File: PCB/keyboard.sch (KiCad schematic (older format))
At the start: 154 parts, among them J1 USB_mini_micro_B, U1 ATMEGA32U4, X1 Crystal_GND24_Small

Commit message: added standard 68 key layout
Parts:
- added D_R_ALT_STD_1: D, acheron_Components:D_SOD-123, symbol Device:D
- added K_BCK_STD1: KEYSW, MX_Only:MXOnly-2U-NoLED, symbol keyboard_parts:KEYSW
- added K_CAPS_STD_2: KEYSW, MX_Only:MXOnly-1.75U-NoLED, symbol keyboard_parts:KEYSW
- added K_CMD_STD_1, K_CMD_STD_3, K_CTRL_STD_1, K_MEN_STD_1, K_R_ALT_STD_1, K_WIN_STD_1: KEYSW, MX_Only:MXOnly-1.25U-NoLED, symbol keyboard_parts:KEYSW
- added K_SPACE_STD1: KEYSW, MX_Only:MXOnly-6.25U-NoLED, symbol keyboard_parts:KEYSW
- K_&lt;I1, K_&lt;I2, K_&lt;I3, K_CTRL1, K_TAB1: footprint MX_Alps_Hybrid:MX-1.5U-NoLED -> MX_Only:MXOnly-1.5U-NoLED
- K_&lt;I_E1, K_0, K_1, K_2, K_3, K_4, K_5, K_6, K_7, K_8, K_9, K_A1, K_B1, K_BSLSH1, K_C1, K_CBRAC1, K_COMMA1, K_D1, K_DELETE1, K_DOT1, K_DOWN1, K_E1, K_END1, K_EQUAL1, K_F1, K_FN1, K_G1, K_H1, K_HOME1, K_I1, K_INSERT1, K_J1, K_K1, K_L1, K_LEFT1, K_M1, K_MINUS1, K_N1, K_O1, K_OBRAC1, K_P1, K_Q1, K_QUOTE1, K_R1, K_RIGHT1, K_S1, K_SEMIC1, K_SLASH1, K_T1, K_U1, K_UP1, K_V1, K_W1, K_X1, K_Y1, K_Z1, K_`1: footprint MX_Alps_Hybrid:MX-1U-NoLED -> MX_Only:MXOnly-1U-NoLED
- K_ALT1, K_CAPS1, K_WIN1: footprint MX_Alps_Hybrid:MX-1.25U-NoLED -> MX_Only:MXOnly-1.25U-NoLED
- K_ENTER1, K_SHIFT2: footprint MX_Alps_Hybrid:MX-2.25U-NoLED -> MX_Only:MXOnly-2.25U-NoLED
- K_SHIFT1: footprint MX_Alps_Hybrid:MX-1.75U-NoLED -> MX_Only:MXOnly-1.75U-NoLED
- K_SPACE1: footprint MX_Alps_Hybrid:MX-7U-NoLED -> MX_Only:MXOnly-7U-NoLED
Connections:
- net col0: now also K_CAPS_STD_2.1, K_CTRL_STD_1.1
- net col11: now also K_R_ALT_STD_1.1
- net col12: now also K_CMD_STD_3.1
- net col13: now also K_BCK_STD1.1
- net col2: now also K_WIN_STD_1.1
- net col3: now also K_CMD_STD_1.1
- net col7: now also K_SPACE_STD1.1
- net at D_CAPS1.2 (A), K_CAPS1.2: now also K_CAPS_STD_2.2
- net at D_CTRL1.2 (A), K_CTRL1.2: now also K_CTRL_STD_1.2
- net at D_WIN1.2 (A), K_WIN1.2: now also K_WIN_STD_1.2
- net at D_&lt;I2.2 (A), K_&lt;I2.2: now also K_CMD_STD_1.2
- net at D_SPACE1.2 (A), K_SPACE1.2: now also K_SPACE_STD1.2
- net at D_&lt;I3.2 (A), K_&lt;I3.2: now also K_CMD_STD_3.2
- net at D_ALT1.2 (A), K_ALT1.2: now also K_MEN_STD_1.2
- net at D_BSLSH1.2 (A), K_BSLSH1.2: now also K_BCK_STD1.2
- new net: D_R_ALT_STD_1.2 (A), K_R_ALT_STD_1.2

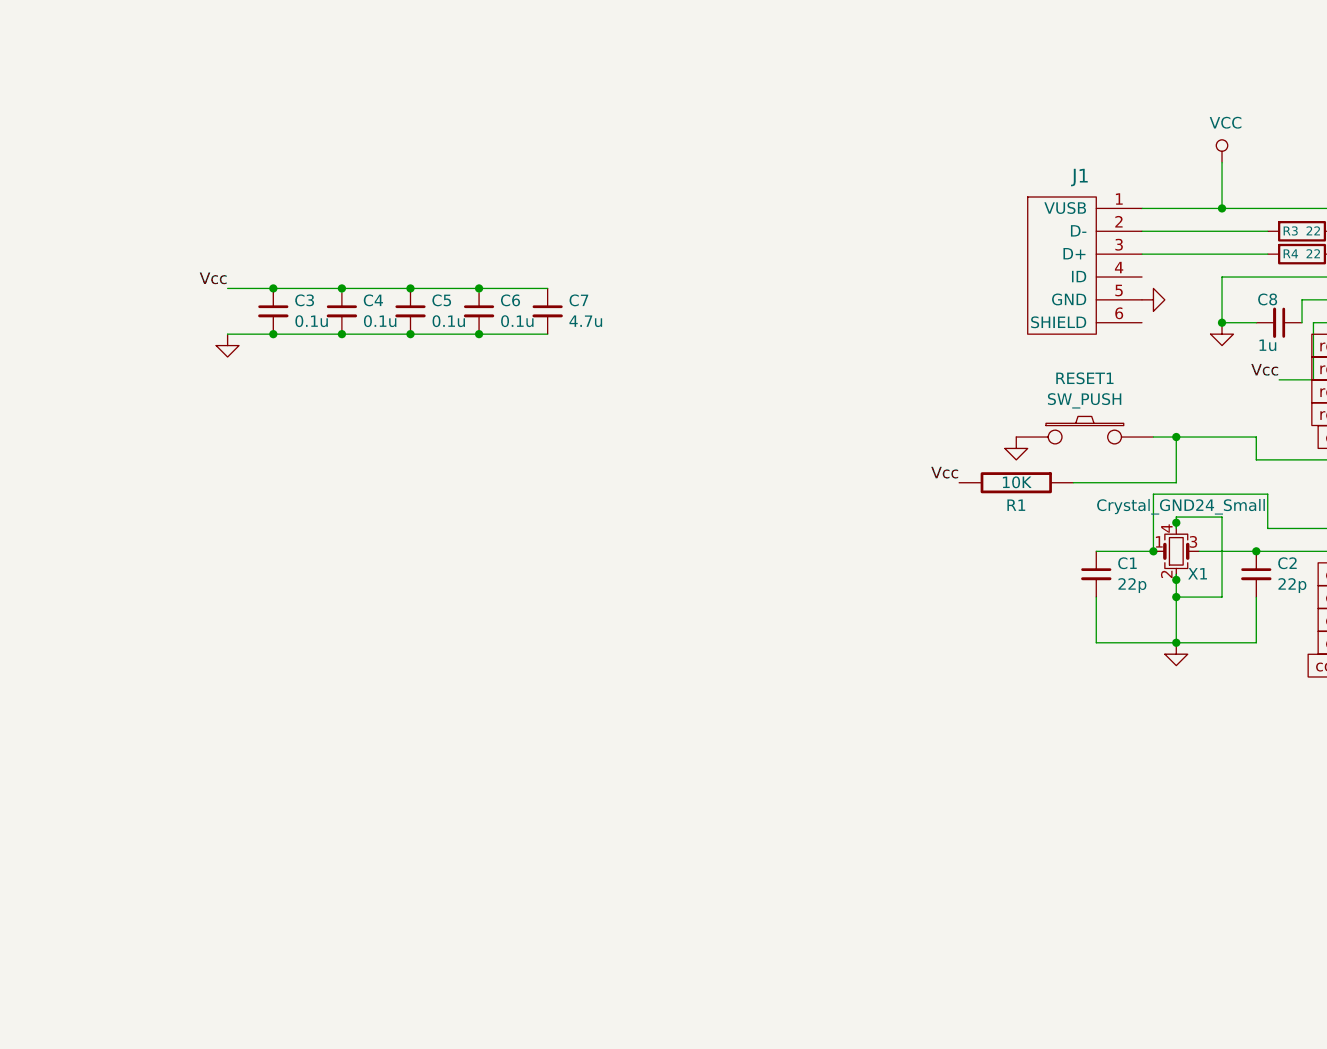
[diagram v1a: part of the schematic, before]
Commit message: added usb type c.
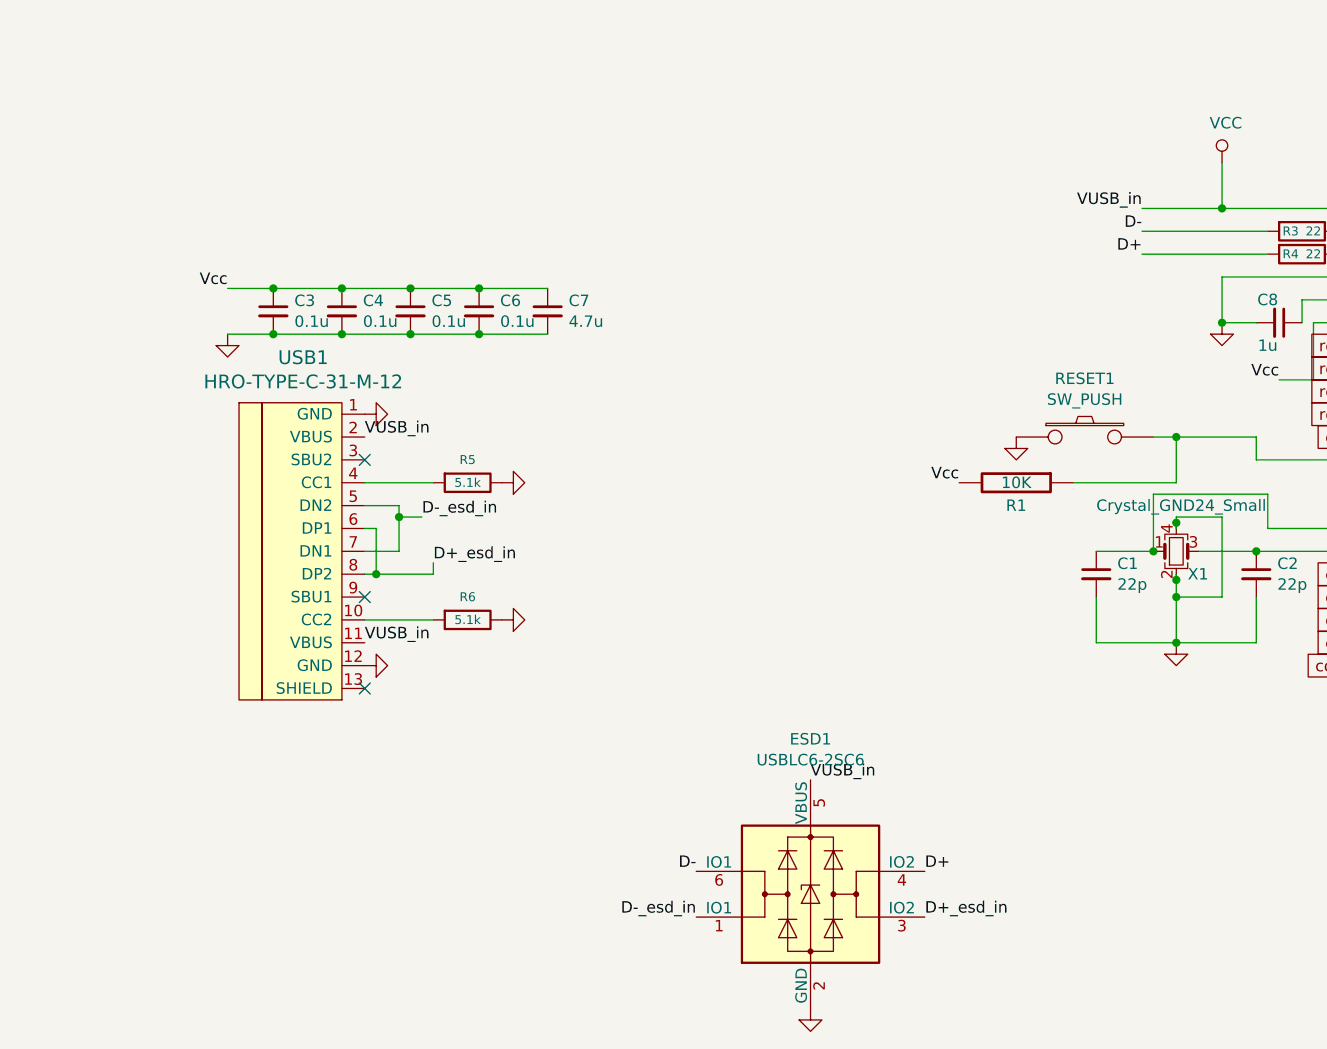
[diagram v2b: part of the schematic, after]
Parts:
- removed J1: USB_mini_micro_B, keyboard_parts:USB_miniB_hirose_5S8, symbol keyboard_parts:USB_mini_micro_B
- added ESD1: USBLC6-2SC6, Package_TO_SOT_SMD:SOT-23-6, symbol Power_Protection_esd:USBLC6-2SC6
- added R5, R6: 5.1k, Resistor_SMD:R_0805_2012Metric_Pad1.15x1.40mm_HandSolder, symbol Device:R
- added USB1: HRO-TYPE-C-31-M-12, usbc_footprint:HRO-TYPE-C-31-M-12, symbol Type-C:HRO-TYPE-C-31-M-12
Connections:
- net GND: now also ESD1.2 (GND), R5.1, R6.1, USB1.1 (GND), USB1.12 (GND)
- net VCC: now also ESD1.5 (VBUS), USB1.11 (VBUS), USB1.2 (VBUS)
- net D-: now reaches R3.2
- net D-: now also ESD1.6 (IO1)
- net D+: now reaches R4.2
- net D+: now also ESD1.4 (IO2)
- new net: R5.2, USB1.4 (CC1)
- new net: R6.2, USB1.10 (CC2)
- new net D+_esd_in: ESD1.3 (IO2), USB1.6 (DP1), USB1.8 (DP2)
- new net D-_esd_in: ESD1.1 (IO1), USB1.5 (DN2), USB1.7 (DN1)
- no-connect marks 4 -> 7
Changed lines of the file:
@@
 col16
-$Comp
-L keyboard_parts:USB_mini_micro_B J1
-U 1 1 000014A1
-P 6350 7200
-F 0 "J1" H 6232 7491 60  0000 C CNN
-F 1 "USB_mini_micro_B" H 6200 7400 60  0001 C CNN
-F 2 "keyboard_parts:USB_miniB_hirose_5S8" H 6300 7200 60  0001 C CNN
-F 3 "" H 6300 7200 60  0000 C CNN
-	1    6350 7200
-	1    0    0    -1
-$EndComp
 $Comp
 L Device:R R3
@@
 Text Label 7100 7800 2    50   ~ 0
 Vcc
-$Comp
-L component:GND #PWR0110
-U 1 1 5DE306C9
-P 6550 7450
-F 0 "#PWR0110" H 6550 7450 30  0001 C CNN
-F 1 "GND" H 6550 7380 30  0001 C CNN
-F 2 "" H 6550 7450 50  0001 C CNN
-F 3 "" H 6550 7450 50  0001 C CNN
-	1    6550 7450
-	0    -1   -1   0
-$EndComp
 Wire Wire Line
 	6500 7050 6850 7050
@@
 	14150 750  14150 1000
 Connection ~ 14150 1000
+Wire Wire Line
+	3250 8350 3250 8400
+Wire Wire Line
+	3250 8400 3350 8400
+Connection ~ 3250 8400
+Wire Wire Line
+	3100 8850 3400 8850
+Wire Wire Line
+	3100 8250 3400 8250
+$Comp
+L Power_Protection_esd:USBLC6-2SC6 ESD1
+U 1 1 5DD11E7B
+P 5050 10050
+F 0 "ESD1" H 5050 10728 50  0000 C CNN
+F 1 "USBLC6-2SC6" H 5050 10637 50  0000 C CNN
+F 2 "Package_TO_SOT_SMD:SOT-23-6" H 4300 10450 50  0001 C CNN
+F 3 "" H 5250 10400 50  0001 C CNN
+	1    5050 10050
+	1    0    0    -1
+$EndComp
+Text Label 3350 8400 0    50   ~ 0
+D-_esd_in
+Text Label 3400 8600 0    50   ~ 0
+D+_esd_in
+Text Label 3100 8050 0    50   ~ 0
+VUSB_in
+$Comp
+L Device:R R5
+U 1 1 5DD1505B
+P 3550 8250
+F 0 "R5" V 3450 8250 39  0000 C CNN
+F 1 "5.1k" V 3550 8250 39  0000 C CNN
+F 2 "Resistor_SMD:R_0805_2012Metric_Pad1.15x1.40mm_HandSolder" V 3480 8250 50  0001 C CNN
+F 3 "~" H 3550 8250 50  0001 C CNN
+	1    3550 8250
+	0    1    1    0
+$EndComp
+$Comp
+L Device:R R6
+U 1 1 5DD3A6B4
+P 3550 8850
+F 0 "R6" V 3450 8850 39  0000 C CNN
+F 1 "5.1k" V 3550 8850 39  0000 C CNN
+F 2 "Resistor_SMD:R_0805_2012Metric_Pad1.15x1.40mm_HandSolder" V 3480 8850 50  0001 C CNN
+F 3 "~" H 3550 8850 50  0001 C CNN
+	1    3550 8850
+	0    1    1    0
+$EndComp
+$Comp
+L component:GND #PWR0112
+U 1 1 5DD635D1
+P 3750 8250
+F 0 "#PWR0112" H 3750 8250 30  0001 C CNN
+F 1 "GND" H 3750 8180 30  0001 C CNN
+F 2 "" H 3750 8250 50  0001 C CNN
+F 3 "" H 3750 8250 50  0001 C CNN
+	1    3750 8250
+	0    -1   -1   0
+$EndComp
+$Comp
+L component:GND #PWR0113
+U 1 1 5DD6393D
+P 3750 8850
+F 0 "#PWR0113" H 3750 8850 30  0001 C CNN
+F 1 "GND" H 3750 8780 30  0001 C CNN
+F 2 "" H 3750 8850 50  0001 C CNN
+F 3 "" H 3750 8850 50  0001 C CNN
+	1    3750 8850
+	0    -1   -1   0
+$EndComp
+Text Label 5050 9550 0    50   ~ 0
+VUSB_in
+Text Label 4550 10150 2    50   ~ 0
+D-_esd_in
+Text Label 5550 10150 0    50   ~ 0
+D+_esd_in
+Text Label 5550 9950 0    50   ~ 0
+D+
+Text Label 4550 9950 2    50   ~ 0
+D-
+$Comp
+L component:GND #PWR0114
+U 1 1 5DDD86B6
+P 5050 10600
+F 0 "#PWR0114" H 5050 10600 30  0001 C CNN
+F 1 "GND" H 5050 10530 30  0001 C CNN
+F 2 "" H 5050 10600 50  0001 C CNN
+F 3 "" H 5050 10600 50  0001 C CNN
+	1    5050 10600
+	1    0    0    -1
+$EndComp
+Text Label 6500 7150 2    50   ~ 0
+D-
+Text Label 6500 7250 2    50   ~ 0
+D+
+Text Label 6500 7050 2    50   ~ 0
+VUSB_in
+$Comp
+L Type-C:HRO-TYPE-C-31-M-12 USB1
+U 1 1 5DE2A8C5
+P 3000 8500
+F 0 "USB1" H 2831 9297 60  0000 C CNN
+F 1 "HRO-TYPE-C-31-M-12" H 2831 9191 60  0000 C CNN
+F 2 "usbc_footprint:HRO-TYPE-C-31-M-12" H 3000 8500 60  0001 C CNN
+F 3 "" H 3000 8500 60  0001 C CNN
+	1    3000 8500
+	1    0    0    -1
+$EndComp
+Wire Wire Line
+	3100 8350 3250 8350
+Wire Wire Line
+	3250 8400 3250 8550
+Wire Wire Line
+	3100 8450 3150 8450
+Wire Wire Line
+	3150 8650 3100 8650
+Wire Wire Line
+	3100 8550 3250 8550
+Wire Wire Line
+	3150 8450 3150 8550
+Wire Wire Line
+	3150 8550 3150 8650
+Text Label 3100 8950 0    50   ~ 0
+VUSB_in
+$Comp
+L component:GND #PWR0110
+U 1 1 5DFAA80B
+P 3150 9050
+F 0 "#PWR0110" H 3150 9050 30  0001 C CNN
+F 1 "GND" H 3150 8980 30  0001 C CNN
+F 2 "" H 3150 9050 50  0001 C CNN
+F 3 "" H 3150 9050 50  0001 C CNN
+	1    3150 9050
+	0    -1   -1   0
+$EndComp
+$Comp
+L component:GND #PWR0115
+U 1 1 5DFAAF61
+P 3150 7950
+F 0 "#PWR0115" H 3150 7950 30  0001 C CNN
+F 1 "GND" H 3150 7880 30  0001 C CNN
+F 2 "" H 3150 7950 50  0001 C CNN
+F 3 "" H 3150 7950 50  0001 C CNN
+	1    3150 7950
+	0    -1   -1   0
+$EndComp
+NoConn ~ 3100 8150
+NoConn ~ 3100 8750
+NoConn ~ 3100 9150
+Wire Wire Line
+	3150 8650 3400 8650
+Wire Wire Line
+	3400 8650 3400 8600
+Connection ~ 3150 8650
 $EndSCHEMATC
